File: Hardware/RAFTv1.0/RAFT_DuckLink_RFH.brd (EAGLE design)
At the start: 160 x 100 mm, 144 parts, among them J1 AMPHENOL_132134, J2 AMPHENOL_132134, J4 Micro-USB, J5 132134-15, J6 S2B-PH-K-S(LF)(SN), Q1 SIA817EDJ, Q2 SI7288DP, Q4 SI7288DP, U1 SX1276, U10 PE4259, U2 MAX2771ETI+, U3 ESP32-D0WD, U4 W25Q16BVSSIG, U5 INTERFACE-CP2102-GMR(QFN28), U6 PE4259, U7 SP0503BAHT, U8 BQ24650RVAR, U9 TPS63070RNMT, Y1 32.768kHz

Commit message: added uart to board layout
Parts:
- moved C57 219.4 mm to (138.4, 25.7)
- moved C56 216.6 mm to (138.4, 26.9)
- moved D5 213.9 mm to (144.0, 37.6), turned to 90 degrees
- moved C55 213.0 mm to (138.4, 32.5), turned to 270 degrees
- moved C54 204.0 mm to (136.9, 32.5), turned to 270 degrees
- moved R9 176.6 mm to (131.6, 34.3), turned to 180 degrees
- moved J4 17.8 mm to (153.7, 29.2)
- moved U7 17.8 mm to (145.5, 29.7)
- moved U5 16.3 mm to (133.1, 30.0), turned to 180 degrees
- moved J3 5.89 mm to (81.0, 6.35)
- moved C36 0.57 mm to (90.0, 51.8)
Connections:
- removed net N$56: J4.5, J4.P$1, J4.P$2, J4.P$8, J4.P$9, U7.1
- net GND: now also J4.5, J4.P$1, J4.P$2, J4.P$8, J4.P$9, U7.1
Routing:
- net +5V: track 0.00 -> 33.1 mm
- net GND: track 5.78 -> 33.5 mm, vias 11 -> 19
- net N$55: track 0.00 -> 20.2 mm, vias 0 -> 2
- net N$54: track 0.00 -> 18.8 mm, vias 0 -> 2
- net N$53: track 0.00 -> 8.25 mm
- net N$51: track 0.00 -> 2.51 mm
- net !RST: track 0.00 -> 2.05 mm, vias 0 -> 1
- net U0RXD: track 7.29 -> 9.33 mm, vias 1 -> 2
- net U0TXD: track 0.73 -> 2.59 mm, vias 1 -> 2
- net +3.3V: track 23.7 -> 24.3 mm

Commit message: battery charger/power distribution layouts
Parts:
- added J8: POWER_JACK, SparkFun-Connectors:POWER_JACK_PTH
- D6: value 150060RS75000 -> LTST-C190GKT; device WL-SMCW:WL-SMCW_0603 -> LTST-C190GKT:0603
- R21: value 165R -> 10K; device RAFT-components:RESC3116X60N -> CRCW040210K0JNED:RESC1005X40N
- moved D6 247.6 mm to (128.0, 81.5), turned to 180 degrees
- moved R21 244.4 mm to (127.3, 83.8), turned to 270 degrees
- moved J6 237.5 mm to (153.7, 54.9), turned to 90 degrees
- moved J7 237.1 mm to (124.2, 81.8), turned to 90 degrees
- moved C58 208.6 mm to (128.1, 44.1), turned to 90 degrees
- moved C60 206.7 mm to (133.6, 46.5)
- moved D4 205.4 mm to (132.3, 40.9)
- moved Q2 203.6 mm to (127.8, 56.4)
- moved R26 202.8 mm to (135.1, 44.7), turned to 270 degrees
- moved U9 201.2 mm to (126.7, 69.1), turned to 270 degrees
- moved Q1 198.5 mm to (126.7, 63.0), turned to 180 degrees
- moved C61 198.4 mm to (122.1, 59.9), turned to 90 degrees
- moved R25 198.3 mm to (133.1, 44.7), turned to 90 degrees
- moved R27 198.1 mm to (130.6, 70.6), turned to 90 degrees
- moved D1 196.3 mm to (134.9, 58.2), turned to 270 degrees
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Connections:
- net GND: now also D6.1, J8.GND, J8.GNDBREAK; no longer D6.2
- net N$52: now also D6.2; no longer D6.1
- net VIN: now also J8.PWR
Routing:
- net GND: track 33.5 -> 64.2 mm, vias 19 -> 39
- net +3V3: track 0.00 -> 14.6 mm
- net N$57: track 0.00 -> 6.92 mm
- net SC_VIN: track 0.00 -> 6.89 mm
- net VIN_SYS: track 0.00 -> 6.67 mm
- net V_BAT: track 0.00 -> 6.61 mm
- net N$61: track 0.00 -> 6.17 mm
- net N$47: track 0.00 -> 5.33 mm
- net N$49: track 0.00 -> 4.25 mm
- net N$60: track 0.00 -> 3.92 mm
- net N$62: track 0.00 -> 3.87 mm
- net N$29: track 0.00 -> 2.29 mm
- net PACK_THERM: track 0.00 -> 1.99 mm
- net N$69: track 0.00 -> 1.61 mm
- net N$63: track 0.00 -> 1.58 mm
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
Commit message: preliminary board layout
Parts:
- moved R24 190.3 mm to (125.6, 35.6), turned to 90 degrees
- moved R23 185.2 mm to (123.2, 36.6), turned to 90 degrees
- moved S2 171.5 mm to (114.3, 38.9), turned to 180 degrees
- moved R8 169.4 mm to (133.1, 36.1), turned to 180 degrees
- moved C73 161.2 mm to (128.5, 23.1), turned to 180 degrees
- moved U$1 158.4 mm to (81.8, 51.8), turned to 180 degrees
- moved C72 156.2 mm to (126.2, 24.4), turned to 270 degrees
- moved S1 155.2 mm to (114.3, 30.0), turned to 180 degrees
- moved C22 154.9 mm to (81.5, 11.2), turned to 180 degrees
- moved C23 148.4 mm to (71.9, 11.4), turned to 180 degrees
- moved C17 148.4 mm to (79.2, 16.5), turned to 180 degrees
- moved C25 146.9 mm to (67.6, 16.8)
- moved C43 146.1 mm to (68.6, 71.6), turned to 90 degrees
- moved C24 144.0 mm to (67.6, 18.0)
- moved C27 143.5 mm to (62.5, 19.3), turned to 180 degrees
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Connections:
- net 2G4_INT_ANT: now also U10.3; no longer U10.1
- net N$70: now also U10.1; no longer U10.3
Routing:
- net VIN: track 0.00 -> 73.6 mm
- net +3.3V: track 25.2 -> 67.7 mm, vias 5 -> 13
- net GND: track 64.2 -> 106.6 mm, vias 39 -> 72
- net V_BAT: track 6.61 -> 42.3 mm, vias 0 -> 4
- net N$63: track 1.58 -> 37.0 mm, vias 0 -> 2
- net CHIP_PU: track 0.00 -> 28.9 mm
- net 2G4_ANT_SEL: track 0.00 -> 21.7 mm, vias 0 -> 2
- net N$59: track 0.00 -> 20.4 mm, vias 0 -> 2
- net +3V3: track 14.6 -> 34.8 mm, vias 0 -> 1
- net N$37: track 0.00 -> 18.5 mm, vias 0 -> 2
- net DTR: track 0.00 -> 17.2 mm
- net N$44: track 0.00 -> 16.2 mm
- net N$34: track 0.68 -> 16.4 mm
- net N$39: track 0.00 -> 15.5 mm
- net N$61: track 6.17 -> 20.1 mm
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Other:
- board size 160 x 100 mm -> 155.7 x 127 mm

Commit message: power added to bottom layer
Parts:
- moved C16 161.8 mm to (-65.8, 98.8)
- moved C17 161.8 mm to (-58.4, 101.6)
- moved C18 161.8 mm to (-68.3, 98.8)
- moved C19 161.8 mm to (-58.4, 107.7)
- moved C20 161.8 mm to (-63.5, 98.3)
- moved C21 161.8 mm to (-68.1, 106.9)
- moved C22 161.8 mm to (-56.1, 96.3)
- moved C23 161.8 mm to (-65.8, 96.5)
- moved C24 161.8 mm to (-70.1, 103.1)
- moved C25 161.8 mm to (-70.1, 101.9)
- moved C26 161.8 mm to (-72.2, 106.9)
- moved C27 161.8 mm to (-75.2, 104.4)
- moved C28 161.8 mm to (-77.0, 102.4)
- moved C29 161.8 mm to (-80.5, 102.4)
- moved C30 161.8 mm to (-84.1, 102.4)
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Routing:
- net V_BAT: track 42.3 -> 37.3 mm

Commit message: nearly complete board layout
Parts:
- moved J1 184.0 mm to (67.8, 12.2), turned to 90 degrees
- moved L6 170.1 mm to (60.7, 12.2), turned to 0 degrees
- moved C30 169.9 mm to (61.0, 13.9), turned to 270 degrees
- moved C29 165.9 mm to (59.0, 12.6), turned to 270 degrees
- moved L5 161.6 mm to (56.9, 16.5), turned to 270 degrees
- moved C28 157.7 mm to (56.5, 18.3), turned to 0 degrees
- moved C27 156.7 mm to (56.9, 20.1), turned to 270 degrees
- moved L3 153.2 mm to (56.9, 22.6), turned to 270 degrees
- moved C26 152.9 mm to (56.5, 24.4), turned to 180 degrees
- moved C25 150.0 mm to (59.4, 26.2), turned to 90 degrees
- moved C24 149.6 mm to (58.2, 26.2), turned to 90 degrees
- moved L2 149.2 mm to (56.9, 26.2), turned to 90 degrees
- moved C18 148.8 mm to (62.5, 27.9), turned to 270 degrees
- moved C23 146.3 mm to (64.8, 30.5), turned to 270 degrees
- moved C21 145.6 mm to (54.4, 28.2), turned to 0 degrees
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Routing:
- net N$43: track 1.82 -> 9.14 mm
- net V_BAT: track 37.3 -> 42.6 mm

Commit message: mostly good board design
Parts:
- moved C21 4.58 mm to (52.5, 24.0)
- moved R3 3.88 mm to (63.0, 34.5)
- moved J3 3.81 mm to (68.6, 53.1)
- moved C10 3.77 mm to (16.4, 65.9), turned to 90 degrees
- moved C19 3.75 mm to (51.8, 34.5)
- moved J1 3.75 mm to (66.0, 8.89)
- moved C22 3.66 mm to (63.0, 37.1)
- moved L3 3.64 mm to (55.4, 19.3)
- moved C28 3.64 mm to (55.0, 15.0)
- moved L5 3.64 mm to (55.4, 13.2)
- moved C25 3.64 mm to (57.9, 22.9)
- moved C26 3.64 mm to (55.0, 21.1)
- moved C27 3.64 mm to (55.4, 16.8)
- moved C29 3.64 mm to (57.5, 9.30)
- moved C30 3.64 mm to (59.5, 10.6)
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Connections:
- net +3.3V: now also J3.16, J3.18
- net +3V3: no longer J3.16, J3.18
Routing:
- net +5V: track 33.1 -> 178.1 mm
- net GPS_ANT_SEL: track 3.84 -> 59.0 mm, vias 1 -> 2
- net GND: track 106.3 -> 137.4 mm, vias 72 -> 93
- net GPS_INT_ANT: track 0.00 -> 25.3 mm
- net +3.3V: track 67.7 -> 92.0 mm, vias 13 -> 19
- net 2G4_INT_ANT: track 0.00 -> 23.7 mm
- net SX_RST: track 5.00 -> 26.7 mm, vias 1 -> 0
- net N$70: track 0.00 -> 11.9 mm
- net N$17: track 0.00 -> 10.4 mm
- net N$7: track 0.00 -> 9.93 mm
- net N$16: track 0.00 -> 8.39 mm
- net N$31: track 0.00 -> 7.25 mm
- net N$21: track 0.00 -> 6.43 mm
- net N$15: track 0.00 -> 6.40 mm
- net N$12: track 0.00 -> 6.32 mm
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- added copper zone on layer 15, net +3.3V
- added copper zone on layer 2, net GND
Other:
- board size 155.7 x 127 mm -> 73.7 x 83.8 mm

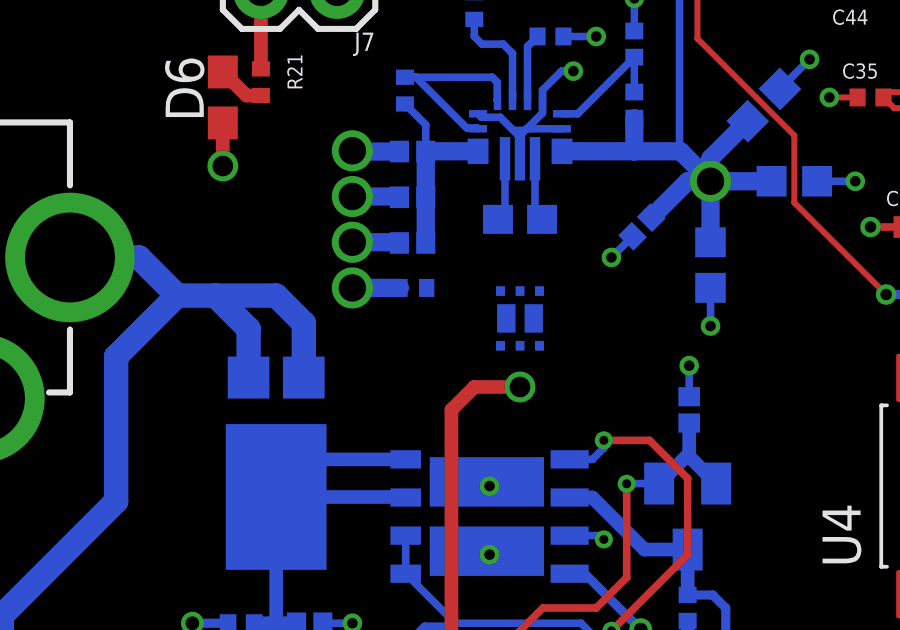
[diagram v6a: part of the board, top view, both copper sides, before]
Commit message: fixed mosfet
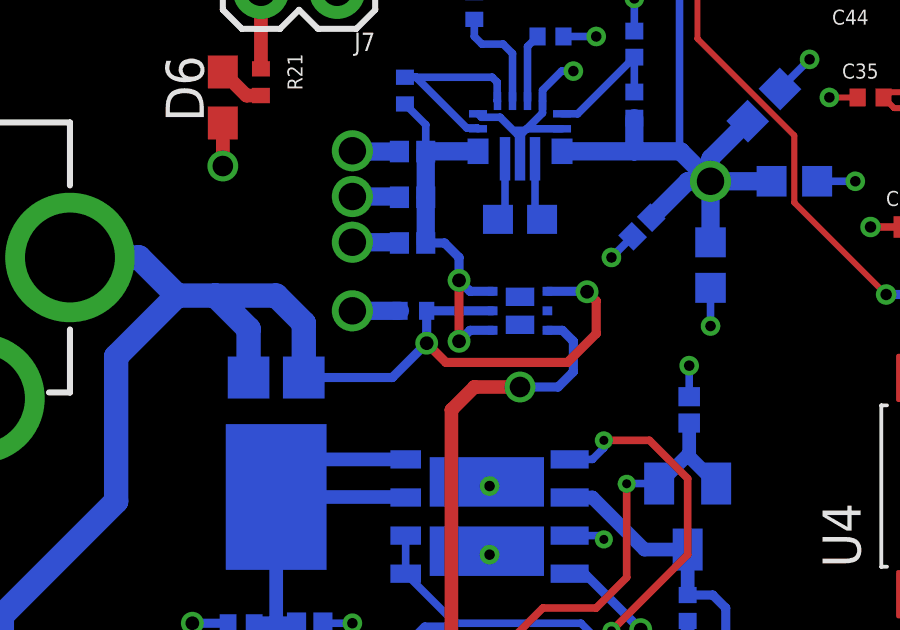
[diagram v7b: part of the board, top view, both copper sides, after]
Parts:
- Q1: device RAFT-components:SC70-6L-DUAL -> RAFT-components:POWERPAKSC-70
- moved R19 0.76 mm to (25.4, 43.4)
- moved Q1 0.25 mm to (29.0, 43.4), turned to 0 degrees
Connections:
- net VIN: now also Q1.1, Q1.5; no longer Q1.P$1, Q1.P$5
- net VIN_SYS: now also Q1.4, Q1.6; no longer Q1.P$4, Q1.P$6
- net V_BAT: now also Q1.3; no longer Q1.P$3
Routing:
- net VIN: track 73.8 -> 90.8 mm, vias 0 -> 2
- net VIN_SYS: track 6.68 -> 13.3 mm, vias 0 -> 2
- net V_BAT: track 42.6 -> 46.6 mm
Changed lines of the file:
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@@
 <attribute name="VALUE" x="27.466" y="45.016" size="0.5" layer="28" rot="MR180" align="top-left"/>
 </element>
-<element name="Q1" library="RAFT-components" package="SC70-6L-DUAL" value="SIA817EDJ" x="28.956" y="43.18" smashed="yes" rot="MR180" grouprefs="POWER"/>
 <element name="Q2" library="RAFT-components" package="POWERPAK-SO8_1" value="SI7288DP" x="27.94" y="36.576" smashed="yes" rot="MR0" grouprefs="POWER">
 <attribute name="ALLIED_NUMBER" value="70459563" x="-44.45" y="17.526" size="1.778" layer="28" rot="MR0" display="off"/>
@@
 <attribute name="VALUE" x="51.7956" y="44.3686" size="0.5" layer="27" rot="R270" align="top-left"/>
 </element>
-<element name="R19" library="RAFT-components" package="RESC1005X40N" value="100k" x="25.4" y="44.196" smashed="yes" rot="MR180" grouprefs="POWER">
-<attribute name="DESCRIPTION" value=" 100 kOhms ±1% 0.063W, 1/16W Chip Resistor 0402 _1005 Metric_ Automotive AEC-Q200 Thick Film " x="80.01" y="122.936" size="1.778" layer="28" rot="MR180" display="off"/>
-<attribute name="DIGI-KEY_PART_NUMBER" value="541-100KLCT-ND" x="80.01" y="122.936" size="1.778" layer="28" rot="MR180" display="off"/>
-<attribute name="DIGI-KEY_PURCHASE_URL" value="https://www.digikey.com/product-detail/en/vishay-dale/CRCW0402100KFKED/541-100KLCT-ND/1183351?utm_source=snapeda&amp;utm_medium=aggregator&amp;utm_campaign=symbol" x="80.01" y="122.936" size="1.778" layer="28" rot="MR180" display="off"/>
-<attribute name="MF" value="Vishay" x="80.01" y="122.936" size="1.778" layer="28" rot="MR180" display="off"/>
-<attribute name="MP" value="CRCW0402100KFKED" x="80.01" y="122.936" size="1.778" layer="28" rot="MR180" display="off"/>
-<attribute name="NAME" x="24.45" y="43.566" size="0.5" layer="26" rot="MR180"/>
-<attribute name="PACKAGE" value="1005 Panasonic Electronic Components" x="80.01" y="122.936" size="1.778" layer="28" rot="MR180" display="off"/>
-<attribute name="VALUE" x="24.45" y="42.54" size="0.5" layer="28" rot="MR180" align="top-left"/>
+<element name="R19" library="RAFT-components" package="RESC1005X40N" value="100k" x="25.4" y="43.434" smashed="yes" rot="MR180" grouprefs="POWER">
+<attribute name="DESCRIPTION" value=" 100 kOhms ±1% 0.063W, 1/16W Chip Resistor 0402 _1005 Metric_ Automotive AEC-Q200 Thick Film " x="80.01" y="122.174" size="1.778" layer="28" rot="MR180" display="off"/>
+<attribute name="DIGI-KEY_PART_NUMBER" value="541-100KLCT-ND" x="80.01" y="122.174" size="1.778" layer="28" rot="MR180" display="off"/>
+<attribute name="DIGI-KEY_PURCHASE_URL" value="https://www.digikey.com/product-detail/en/vishay-dale/CRCW0402100KFKED/541-100KLCT-ND/1183351?utm_source=snapeda&amp;utm_medium=aggregator&amp;utm_campaign=symbol" x="80.01" y="122.174" size="1.778" layer="28" rot="MR180" display="off"/>
+<attribute name="MF" value="Vishay" x="80.01" y="122.174" size="1.778" layer="28" rot="MR180" display="off"/>
+<attribute name="MP" value="CRCW0402100KFKED" x="80.01" y="122.174" size="1.778" layer="28" rot="MR180" display="off"/>
+<attribute name="NAME" x="25.212" y="44.582" size="0.5" layer="26" rot="MR180"/>
+<attribute name="PACKAGE" value="1005 Panasonic Electronic Components" x="80.01" y="122.174" size="1.778" layer="28" rot="MR180" display="off"/>
+<attribute name="VALUE" x="24.45" y="41.778" size="0.5" layer="28" rot="MR180" align="top-left"/>
 </element>
 <element name="R2" library="rcl-raft" package="RESC1005X40N" value="0R" x="57.531" y="50.419" smashed="yes" rot="R180" grouprefs="MCU">
@@
 <attribute name="PACKAGE" value="0603 Lite-On" x="19.05" y="50.546" size="1.778" layer="27" rot="R90" display="off"/>
 <attribute name="PRICE" value="None" x="19.05" y="50.546" size="1.778" layer="27" rot="R90" display="off"/>
+</element>
+<element name="Q1" library="RAFT-components" package="POWERPAKSC-70" value="SIA817EDJ" x="28.956" y="43.434" smashed="yes" rot="MR0">
+<attribute name="NAME" x="28.278" y="45.086" size="0.3048" layer="26" rot="MR0"/>
+<attribute name="VALUE" x="30.056" y="41.734" size="0.3048" layer="28" rot="MR0"/>
 </element>
 </elements>
@@
 <wire x1="24.9102" y1="45.72" x2="23.368" y2="45.72" width="0.6096" layer="16" grouprefs="POWER"/>
 <via x="23.368" y="45.72" extent="1-16" drill="0.9144" grouprefs="POWER"/>
-<wire x1="24.955" y1="44.196" x2="23.368" y2="44.196" width="0.6096" layer="16" grouprefs="POWER"/>
-<via x="23.368" y="44.196" extent="1-16" drill="0.9144" grouprefs="POWER"/>
+<wire x1="24.955" y1="43.434" x2="23.368" y2="43.434" width="0.6096" layer="16" grouprefs="POWER"/>
+<via x="23.368" y="43.434" extent="1-16" drill="0.9144" grouprefs="POWER"/>
 <wire x1="26.7714" y1="3.302" x2="25.654" y2="3.302" width="0.254" layer="16" grouprefs="POWER"/>
 <via x="25.654" y="3.302" extent="1-16" drill="0.3" grouprefs="POWER"/>
@@
 <wire x1="24.9356" y1="47.2186" x2="24.9356" y2="48.7426" width="0" layer="19" extent="16-16"/>
 <wire x1="23.368" y1="45.72" x2="23.368" y2="47.244" width="0" layer="19" extent="1-1"/>
-<wire x1="24.955" y1="44.196" x2="24.9356" y2="45.6946" width="0" layer="19" extent="16-16"/>
+<wire x1="24.955" y1="43.434" x2="24.9356" y2="45.6946" width="0" layer="19" extent="16-16"/>
 <wire x1="30.48" y1="56.388" x2="32.766" y2="53.848" width="0" layer="19" extent="1-1"/>
 <wire x1="26.416" y1="57.404" x2="30.48" y2="57.65" width="0" layer="19" extent="1-1"/>
@@
 </signal>
 <signal name="VIN">
-<contactref element="Q1" pad="P$5"/>
-<contactref element="Q1" pad="P$1"/>
 <contactref element="D5" pad="3"/>
 <contactref element="D1" pad="1"/>
@@
 <wire x1="16.256" y1="45.212" x2="17.526" y2="43.942" width="0.8128" layer="16" grouprefs="POWER"/>
 <wire x1="13.954" y1="45.212" x2="16.256" y2="45.212" width="0.8128" layer="16"/>
-<wire x1="28.306" y1="42.2675" x2="28.956" y2="44.0925" width="0" layer="19" extent="16-16"/>
-<wire x1="25.845" y1="44.196" x2="28.956" y2="44.0925" width="0" layer="19" extent="16-16"/>
-<wire x1="21.748" y1="41.21" x2="25.845" y2="44.196" width="0" layer="19" extent="16-16"/>
+<contactref element="Q1" pad="5"/>
+<contactref element="Q1" pad="1"/>
+<wire x1="28.0435" y1="43.434" x2="25.845" y2="43.434" width="0.3048" layer="16"/>
+<wire x1="25.845" y1="43.434" x2="25.845" y2="42.355" width="0.3048" layer="16"/>
+<wire x1="24.7" y1="41.21" x2="21.748" y2="41.21" width="0.3048" layer="16"/>
+<wire x1="25.845" y1="42.355" x2="24.7" y2="41.21" width="0.3048" layer="16"/>
+<via x="25.845" y="42.355" extent="1-16" drill="0.4572"/>
+<wire x1="25.845" y1="42.355" x2="26.48685" y2="41.71315" width="0.3048" layer="1"/>
+<wire x1="30.53715" y1="41.71315" x2="31.496" y2="42.672" width="0.3048" layer="1"/>
+<wire x1="31.496" y1="42.672" x2="31.496" y2="43.7642" width="0.3048" layer="1"/>
+<wire x1="31.496" y1="43.7642" x2="31.1912" y2="44.069" width="0.3048" layer="1"/>
+<via x="31.1912" y="44.069" extent="1-16" drill="0.4572"/>
+<wire x1="31.1912" y1="44.069" x2="31.1762" y2="44.084" width="0.3048" layer="16"/>
+<wire x1="31.1762" y1="44.084" x2="29.8685" y2="44.084" width="0.3048" layer="16"/>
+<wire x1="26.48685" y1="41.71315" x2="30.53715" y2="41.71315" width="0.3048" layer="1"/>
 </signal>
 <signal name="VIN_SYS">
-<contactref element="Q1" pad="P$4"/>
-<contactref element="Q1" pad="P$6"/>
 <contactref element="R27" pad="1"/>
 <contactref element="C51" pad="1"/>
@@
 <wire x1="25.8136" y1="48.7426" x2="25.8136" y2="47.2186" width="0.6096" layer="16" grouprefs="POWER"/>
 <wire x1="25.8136" y1="47.2186" x2="25.8136" y2="45.6946" width="0.6096" layer="16" grouprefs="POWER"/>
-<wire x1="28.306" y1="44.0925" x2="29.606" y2="44.0925" width="0" layer="19" extent="16-16"/>
-<wire x1="25.8136" y1="45.6946" x2="28.306" y2="44.0925" width="0" layer="19" extent="16-16"/>
+<contactref element="Q1" pad="4"/>
+<contactref element="Q1" pad="6"/>
+<wire x1="25.8136" y1="45.6946" x2="26.4414" y2="45.6946" width="0.3048" layer="16"/>
+<wire x1="26.4414" y1="45.6946" x2="26.924" y2="45.212" width="0.3048" layer="16"/>
+<wire x1="26.924" y1="45.212" x2="26.924" y2="44.45" width="0.3048" layer="16"/>
+<wire x1="27.29" y1="44.084" x2="26.924" y2="44.45" width="0.3048" layer="16"/>
+<wire x1="27.29" y1="44.084" x2="28.0435" y2="44.084" width="0.3048" layer="16"/>
+<via x="26.924" y="44.45" extent="1-16" drill="0.4572"/>
+<wire x1="26.924" y1="44.45" x2="26.924" y2="42.418" width="0.3048" layer="1"/>
+<via x="26.924" y="42.418" extent="1-16" drill="0.4572"/>
+<wire x1="26.924" y1="42.418" x2="27.29" y2="42.784" width="0.3048" layer="16"/>
+<wire x1="27.29" y1="42.784" x2="28.0435" y2="42.784" width="0.3048" layer="16"/>
 </signal>
 <signal name="N$29">
@@
 <contactref element="C66" pad="2"/>
 <contactref element="C65" pad="2"/>
-<contactref element="Q1" pad="P$3"/>
 <wire x1="13.5198" y1="28.125" x2="13.5128" y2="28.118" width="0.254" layer="16" grouprefs="POWER"/>
 <wire x1="18.545" y1="30.3308" x2="18.542" y2="30.3278" width="0.254" layer="16" grouprefs="POWER"/>
@@
 <wire x1="12.208" y1="32.274" x2="6.89" y2="32.274" width="0.4572" layer="1"/>
 <wire x1="6.89" y1="32.274" x2="6.858" y2="32.242" width="0.4572" layer="1"/>
-<wire x1="28.956" y1="40.894" x2="29.606" y2="42.2675" width="0" layer="19" extent="16-16"/>
+<contactref element="Q1" pad="3"/>
+<wire x1="29.8685" y1="42.784" x2="30.368" y2="42.784" width="0.3048" layer="16"/>
+<wire x1="30.368" y1="42.784" x2="30.734" y2="42.418" width="0.3048" layer="16"/>
+<wire x1="30.734" y1="42.418" x2="30.734" y2="41.402" width="0.3048" layer="16"/>
+<wire x1="30.734" y1="41.402" x2="30.226" y2="40.894" width="0.3048" layer="16"/>
+<wire x1="30.226" y1="40.894" x2="28.956" y2="40.894" width="0.3048" layer="16"/>
 </signal>
 <signal name="N$64">

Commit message: autorouted board
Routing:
- net SPI_CLK: track 0.00 -> 124.1 mm, vias 0 -> 3
- net U0TXD: track 2.84 -> 124.7 mm
- net SPI_MOSI: track 0.00 -> 116.5 mm, vias 0 -> 4
- net U0RXD: track 9.80 -> 98.5 mm, vias 2 -> 3
- net GPS_SHDN: track 1.85 -> 81.2 mm, vias 1 -> 2
- net GPS_CS: track 2.72 -> 71.3 mm, vias 1 -> 2
- net SPI_MISO: track 0.00 -> 65.0 mm, vias 0 -> 3
- net CHIP_PU: track 32.1 -> 94.9 mm, vias 1 -> 3
- net GPIO4: track 0.00 -> 46.9 mm, vias 0 -> 2
- net GPIO17: track 2.06 -> 46.8 mm
- net GPIO16: track 0.00 -> 42.6 mm, vias 0 -> 2
- net GPIO15: track 0.00 -> 37.0 mm, vias 0 -> 1
- net GND: track 137.4 -> 173.5 mm
- net DATA_OUT: track 0.00 -> 32.1 mm, vias 0 -> 2
- net CLK_SER: track 0.00 -> 30.7 mm, vias 0 -> 2
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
